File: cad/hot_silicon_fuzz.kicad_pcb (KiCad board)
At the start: 2 copper layers, 119.6 x 65.4 mm, 61 parts, among them J201 JACK_IN, J202 JACK_OUT, J203 CONN_PSU, J204 SW_BYPASS, J205 SW_FAT_A, J206 SW_EQ_A, J207 CONN_SIGNALS_A, J208 CONN_SW_EQ_A, J301 SW_EQ_B, J302 CONN_SIGNALS_B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

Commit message: Corrected pots orientation.
Finished layout.
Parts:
- added C204: 100n, Capacitors_SMD:C_0603, F.Cu at (64.0, 69.2)
- C304, C305, C306, C307, Q305, R307, R308, R311, R312, R313, R314, R315, R316, R317: moved to B.Cu
- J207, J208, J302, J303: footprint Pin_Headers:Pin_Header_Straight_1x06_Pitch2.54mm -> Pin_Headers:Pin_Header_Straight_1x06_Pitch1.27mm
- moved J303 143.2 mm to (138.5, 52.5)
- moved Q304 141.8 mm to (129.1, 83.6), turned to 180 degrees
- moved Q303 135.9 mm to (129.2, 90.8), turned to 180 degrees
- moved J302 135.9 mm to (141.5, 52.5)
- moved D301 129.8 mm to (140.0, 70.0), turned to 180 degrees
- moved R317 129.4 mm to (140.5, 63.8), turned to 270 degrees
- moved Q305 123.4 mm to (140.0, 74.0), turned to 90 degrees
- moved Q302 123.4 mm to (139.0, 90.8)
- moved Q301 121.9 mm to (139.0, 83.2)
- moved C304 119.1 mm to (128.5, 55.8)
- moved C307 118.2 mm to (126.2, 59.8), turned to 180 degrees
- moved C309 115.4 mm to (147.0, 82.0), turned to 270 degrees
- moved C306 114.9 mm to (134.2, 58.5), turned to 90 degrees
- moved R315 113.7 mm to (129.5, 66.8), turned to 180 degrees
- moved C302 112.9 mm to (140.0, 86.8), turned to 270 degrees
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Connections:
- J203 pad 3: +BATT -> VDD
- J207 pad 2: GND -> VSS
- J207 pad 5: GND -> VSS
- R204 pad 1: +BATT -> VDD
- RV301 pad 1: Net-(Q303-Pad2) -> Net-(R307-Pad2)
- RV301 pad 3: Net-(R307-Pad2) -> Net-(Q303-Pad2)
- RV302 pad 1: Net-(R307-Pad2) -> GNDD
- RV302 pad 3: GNDD -> Net-(R307-Pad2)
- RV303 pad 1: /Hot Silicon/EQ_SW_2_2B -> Net-(C307-Pad1)
- RV303 pad 3: Net-(C307-Pad1) -> /Hot Silicon/EQ_SW_2_2B
- RV304 pad 1: Net-(RV303-Pad2) -> GNDD
- RV304 pad 3: GNDD -> Net-(RV303-Pad2)
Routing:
- net GNDD: track 0.00 -> 175.5 mm, vias 0 -> 13
- net VSS: track 0.00 -> 135.8 mm, vias 0 -> 8
- net VAA: track 0.00 -> 134.4 mm, vias 0 -> 5
- net (no net): track 0.00 -> 98.8 mm
- net Net-(C202-Pad1): track 0.00 -> 62.1 mm, vias 0 -> 1
- net Net-(J304-Pad2): track 0.00 -> 53.7 mm, vias 0 -> 1
- net Net-(Q303-Pad2): track 0.00 -> 52.3 mm, vias 0 -> 1
- net VDD: track 0.00 -> 48.7 mm
- net Net-(C201-Pad1): track 0.00 -> 48.5 mm, vias 0 -> 1
- net Net-(C309-Pad1): track 0.00 -> 48.2 mm, vias 0 -> 1
- net Net-(C308-Pad2): track 0.00 -> 45.2 mm, vias 0 -> 1
- net /Hot Silicon/EQ_SW_2_3B: track 0.00 -> 44.3 mm, vias 0 -> 2
- net /CONNECTORS/FX_OUT_A: track 0.00 -> 41.5 mm, vias 0 -> 1
- net /Hot Silicon/FX_IN_B: track 0.00 -> 40.8 mm, vias 0 -> 1
- net /CONNECTORS/AUDIO_IN: track 0.00 -> 39.0 mm, vias 0 -> 1
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- added copper zone on B.Cu, net GNDD
- added copper zone on F.Cu, net GNDD
- added copper zone on B.Cu, net VSS
- added copper zone on F.Cu, net VSS
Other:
- board size 119.6 x 65.4 mm -> 119.3 x 65.4 mm
- net class Default: via_dia 0.6 -> 1.5; via_drill 0.4 -> 0.8
- net class POWER added: clearance 0.2, trace_width 0.5, via_dia 1.5, via_drill 0.8
- board text added: "RANDAGODRON"
- board text added: "hot silicon fuzz"
- board text added: "v01"

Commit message: Exported layout.
Done simulations.
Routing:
- net /Hot Silicon/EQ_SW_2_2B: track 38.2 -> 39.0 mm
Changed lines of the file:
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@@
   (general
     (links 125)
-    (no_connects 39)
-    (area 36.424999 38.274999 155.925001 103.875001)
+    (no_connects 2)
+    (area 14.900001 20.3 159.100001 129.700001)
     (thickness 1.6)
     (drawings 48)
-    (tracks 771)
+    (tracks 772)
     (zones 0)
     (modules 62)
@@
     (visible_elements 7FFFFFFF)
     (pcbplotparams
-      (layerselection 0x00030_80000001)
+      (layerselection 0x00000_80000000)
       (usegerberextensions false)
-      (excludeedgelayer true)
+      (excludeedgelayer false)
       (linewidth 0.100000)
       (plotframeref false)
-      (viasonmask false)
+      (viasonmask true)
       (mode 1)
       (useauxorigin false)
@@
       (psnegative false)
       (psa4output false)
-      (plotreference true)
-      (plotvalue true)
+      (plotreference false)
+      (plotvalue false)
       (plotinvisibletext false)
       (padsonsilk false)
       (subtractmaskfromsilk false)
-      (outputformat 1)
+      (outputformat 4)
       (mirror false)
-      (drillshape 1)
+      (drillshape 0)
       (scaleselection 1)
-      (outputdirectory ""))
+      (outputdirectory ../export/))
   )
   (net 0 "")
@@
   (segment (start 50.960959 59.960959) (end 50.5 59.5) (width 0.25) (layer F.Cu) (net 28))
   (segment (start 59.31 63.6305) (end 59.31 63.948) (width 0.25) (layer F.Cu) (net 28))
+  (segment (start 131.750001 55.060661) (end 131.750001 54) (width 0.25) (layer F.Cu) (net 29))
+  (segment (start 133.75 49.99999) (end 133.75 52.000001) (width 0.25) (layer F.Cu) (net 29))
+  (segment (start 133.75 52.000001) (end 131.750001 54) (width 0.25) (layer F.Cu) (net 29))
+  (segment (start 132.75 48.99999) (end 133.75 49.99999) (width 0.25) (layer F.Cu) (net 29))
   (segment (start 134.249999 63.000001) (end 133.5 63.75) (width 0.25) (layer F.Cu) (net 29))
   (segment (start 136.5 58.75) (end 136.5 60.75) (width 0.25) (layer F.Cu) (net 29))
   (segment (start 136.5 60.75) (end 134.249999 63.000001) (width 0.25) (layer F.Cu) (net 29))
-  (segment (start 131.750001 55.060661) (end 131.750001 49.999989) (width 0.25) (layer F.Cu) (net 29))
   (segment (start 133.499999 48.249991) (end 132.75 48.99999) (width 0.25) (layer B.Cu) (net 29))
   (segment (start 136.5 58.75) (end 135.43934 58.75) (width 0.25) (layer F.Cu) (net 29))
   (segment (start 133.54999 48.2) (end 133.499999 48.249991) (width 0.25) (layer B.Cu) (net 29))
-  (segment (start 131.750001 49.999989) (end 132.000001 49.749989) (width 0.25) (layer F.Cu) (net 29))
   (via (at 132.75 48.99999) (size 1.5) (drill 0.8) (layers F.Cu B.Cu) (net 29))
   (segment (start 135.43934 58.75) (end 131.750001 55.060661) (width 0.25) (layer F.Cu) (net 29))
   (segment (start 133.54999 41.70001) (end 133.54999 48.2) (width 0.25) (layer B.Cu) (net 29))
   (segment (start 134.79 40.46) (end 133.54999 41.70001) (width 0.25) (layer B.Cu) (net 29))
-  (segment (start 132.000001 49.749989) (end 132.75 48.99999) (width 0.25) (layer F.Cu) (net 29))
   (segment (start 132 62.25) (end 132 63.75) (width 0.25) (layer B.Cu) (net 29))
   (segment (start 133.5 63.75) (end 132 63.75) (width 0.25) (layer B.Cu) (net 29))

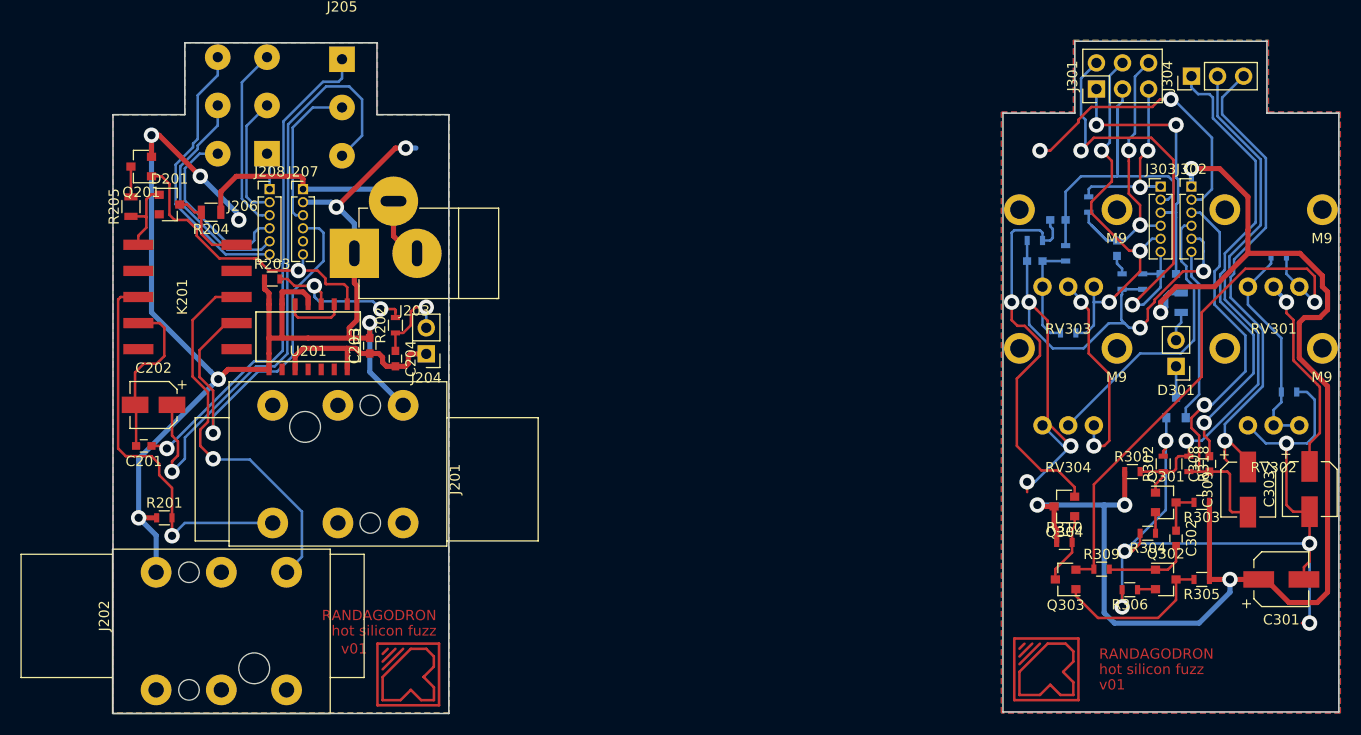
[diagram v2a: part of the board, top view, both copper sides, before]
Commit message: Corrections on layout.
Exported layout.
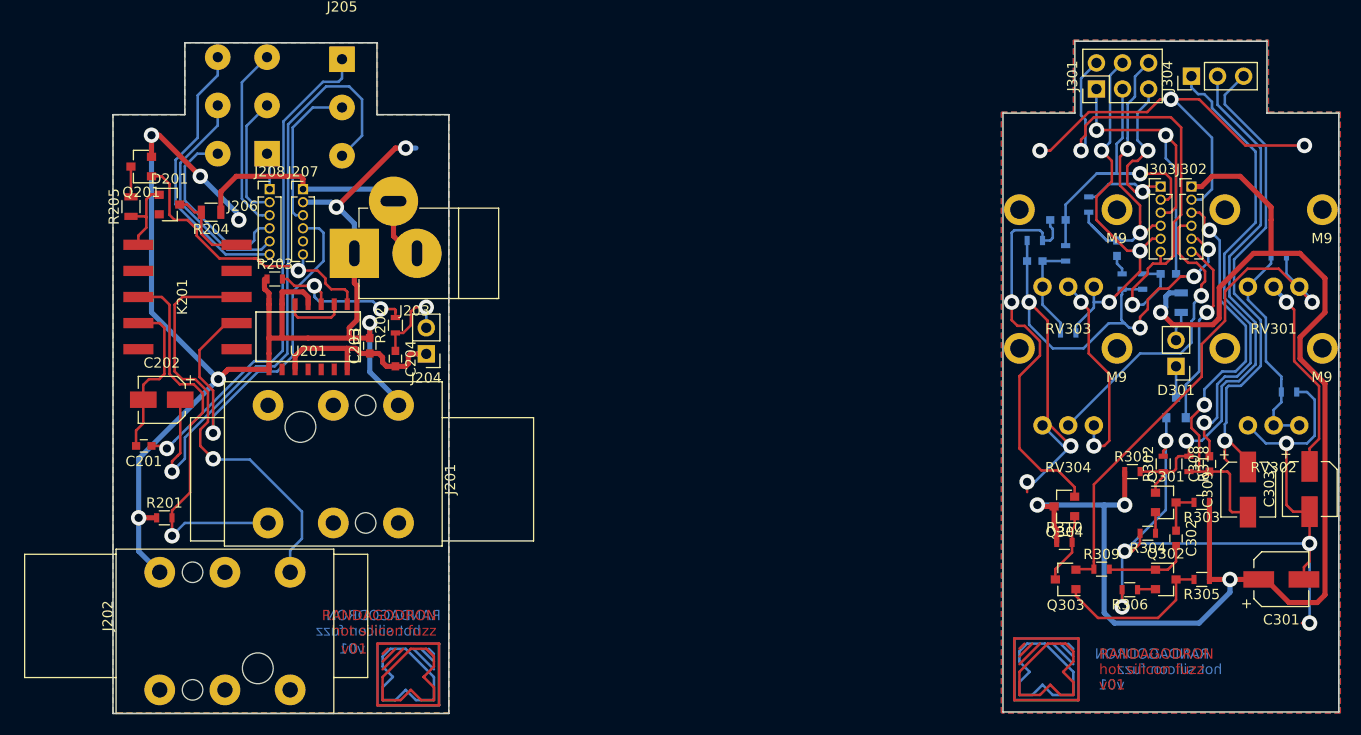
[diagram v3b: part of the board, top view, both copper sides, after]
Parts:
- moved C202 0.94 mm to (41.2, 73.2)
- moved J201 0.45 mm to (68.5, 81.0)
- moved J202 0.35 mm to (36.8, 94.3)
- moved R203 0.25 mm to (52.2, 61.5)
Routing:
- net (no net): track 98.8 -> 197.6 mm
- net GNDD: track 175.5 -> 191.7 mm, vias 13 -> 15
- net /Hot Silicon/EQ_SW_1_3B: track 28.5 -> 34.0 mm
- net /Hot Silicon/EQ_SW_2_3B: track 44.3 -> 49.8 mm
- net /CONNECTORS/AUDIO_OUT: track 37.5 -> 41.4 mm
- net /Hot Silicon/EQ_SW_1_2B: track 34.5 -> 30.8 mm, vias 0 -> 1
- net Net-(Q303-Pad2): track 52.3 -> 50.4 mm
- net /Hot Silicon/FX_OUT_B: track 28.2 -> 30.0 mm, vias 0 -> 1
- net /Hot Silicon/EQ_SW_2_1B: track 28.6 -> 30.0 mm
- net /Hot Silicon/LED_CMD_B: track 17.0 -> 18.3 mm, vias 0 -> 1
- net /Hot Silicon/EQ_SW_1_1B: track 19.8 -> 21.1 mm
- net /Hot Silicon/EQ_SW_2_2B: track 39.0 -> 38.1 mm
- net VAA: track 134.4 -> 135.3 mm, vias 5 -> 4
- net Net-(C307-Pad1): track 10.6 -> 9.97 mm
- net /CONNECTORS/AUDIO_IN: track 39.0 -> 39.5 mm
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
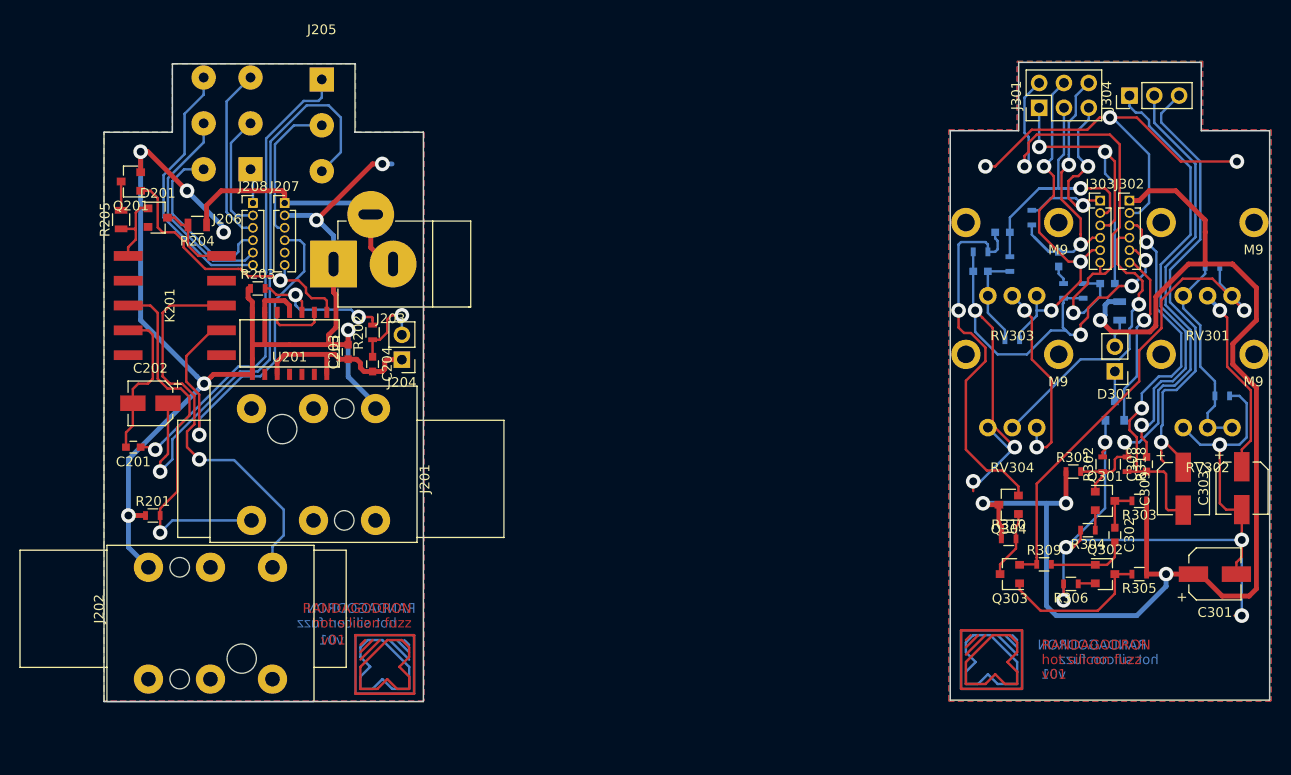
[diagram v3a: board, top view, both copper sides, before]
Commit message: Corrected layout
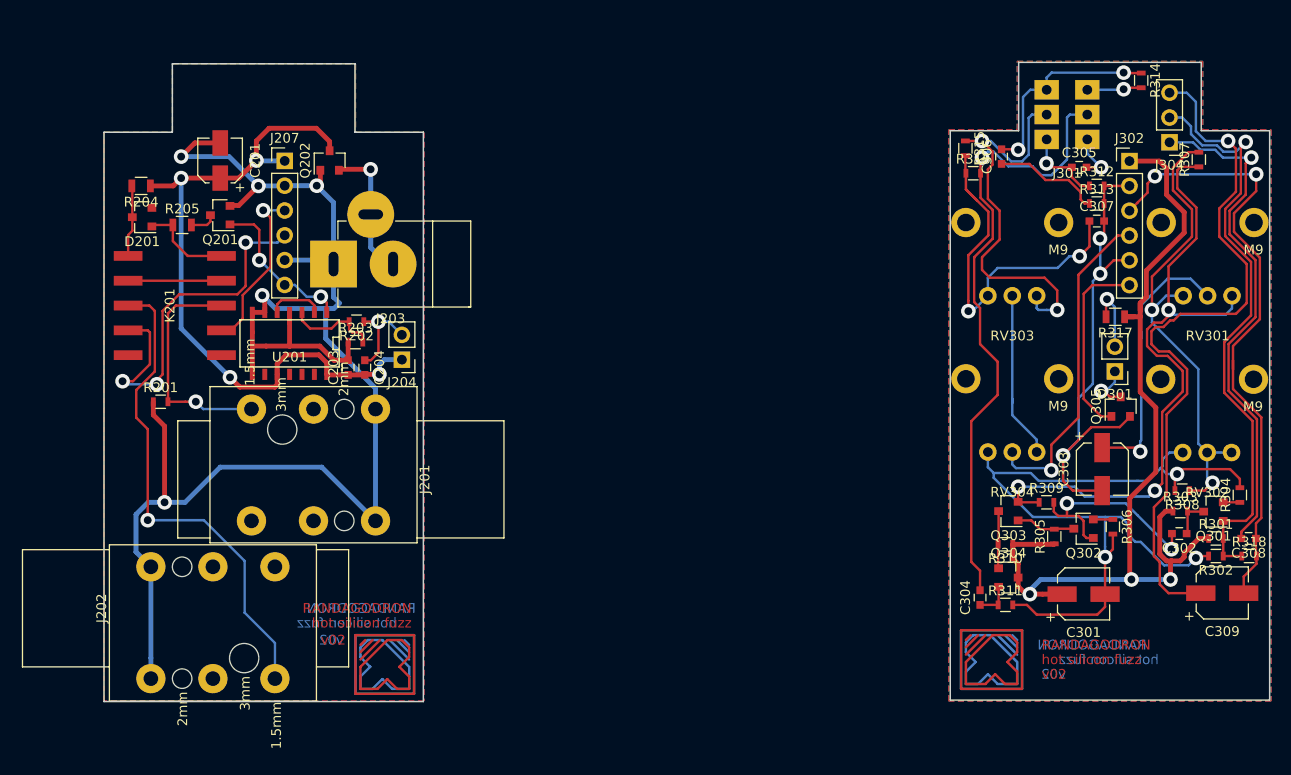
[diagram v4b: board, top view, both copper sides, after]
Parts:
- removed C202: 10u, Capacitors_SMD:CP_Elec_4x4.5
- removed J205: SW_FAT_A, flax_lib:SW_SPDT_through_hole
- removed J206: SW_EQ_A, flax_lib:SW_DPDT_through_hole
- removed J208: CONN_SW_EQ_A, Pin_Headers:Pin_Header_Straight_1x06_Pitch1.27mm
- removed J303: CONN_SW_EQ_B, Pin_Headers:Pin_Header_Straight_1x06_Pitch1.27mm
- added Q202: DTA114E, TO_SOT_Packages_SMD:SOT-23, F.Cu at (59.6, 48.4)
- C201: value 100n -> 10u; footprint Capacitors_SMD:C_0603 -> Capacitors_SMD:CP_Elec_4x4.5
- C304, C305, C306, C307, Q305, R307, R308, R311, R312, R313, R314, R315, R316, R317: moved to F.Cu
- J207, J302: footprint Pin_Headers:Pin_Header_Straight_1x06_Pitch1.27mm -> Pin_Headers:Pin_Header_Straight_1x06_Pitch2.54mm
- J301: footprint Pin_Headers:Pin_Header_Straight_2x03_Pitch2.54mm -> flax_lib:Multicomp_sub-miniature_DPDT
- moved C304 37.5 mm to (126.2, 93.2), turned to 90 degrees
- moved R311 36.2 mm to (128.8, 93.9), turned to 0 degrees
- moved C201 30.7 mm to (48.4, 48.4), turned to 90 degrees
- moved R315 20.2 mm to (124.7, 47.1), turned to 270 degrees
- moved R314 18.0 mm to (142.7, 40.2), turned to 270 degrees
- moved R301 16.1 mm to (150.3, 87.1)
- moved R304 16.0 mm to (152.8, 82.7), turned to 90 degrees
- moved R318 15.6 mm to (153.8, 88.9), turned to 0 degrees
- moved R302 14.9 mm to (150.3, 88.9), turned to 180 degrees
- moved C303 14.4 mm to (138.7, 80.0)
- moved C301 13.6 mm to (136.8, 92.8)
- moved C307 13.0 mm to (138.2, 54.6), turned to 0 degrees
- moved C308 12.9 mm to (153.7, 87.1), turned to 180 degrees
- moved C305 12.2 mm to (136.3, 49.1)
- moved C306 12.0 mm to (128.4, 48.0)
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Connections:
- C201 pad 1: Net-(C201-Pad1) -> VDD
- C201 pad 2: Net-(C201-Pad2) -> VSS
- J203 pad 2: VDD -> Net-(J203-Pad2)
- J203 pad 3: VDD -> Net-(J203-Pad2)
- K201 pad 7: Net-(C201-Pad2) -> /CONNECTORS/FX_IN_A
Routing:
- net Net-(C202-Pad1): track 62.4 -> 0.00 mm, vias 1 -> 0
- net GNDD: track 191.7 -> 138.3 mm, vias 15 -> 6
- net Net-(C201-Pad1): track 48.5 -> 0.00 mm, vias 1 -> 0
- net /Hot Silicon/EQ_SW_2_3B: track 49.8 -> 8.41 mm, vias 2 -> 1
- net VAA: track 135.3 -> 96.8 mm, vias 4 -> 3
- net /Hot Silicon/EQ_SW_1_2B: track 30.8 -> 65.3 mm
- net Net-(C304-Pad1): track 38.2 -> 3.72 mm, vias 1 -> 0
- net /Hot Silicon/EQ_SW_1_3B: track 34.0 -> 4.95 mm, vias 2 -> 1
- net Net-(C307-Pad1): track 9.97 -> 38.2 mm, vias 0 -> 2
- net Net-(R307-Pad2): track 21.6 -> 49.6 mm, vias 0 -> 2
- net /CONNECTORS/EQ_SW_2_3B: track 27.2 -> 0.00 mm
- net Net-(C309-Pad1): track 48.2 -> 73.8 mm
- net VDD: track 48.7 -> 72.3 mm, vias 0 -> 4
- net /Hot Silicon/FX_IN_B: track 40.7 -> 64.1 mm
- net VSS: track 135.9 -> 159.1 mm, vias 8 -> 5
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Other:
- board text added: "v02"
- board text removed: "v01"
